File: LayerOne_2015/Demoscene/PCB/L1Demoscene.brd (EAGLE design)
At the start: 50 x 50 mm, 54 parts, among them IC1 MEGA8-AI, IC2 REG1117, J1 AVR_SPI_PRG_6PTH, J2 CON_HEADER_1X02-PTH

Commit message: 
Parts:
- moved C2 1.02 mm to (9.40, 19.3)
- moved R28 0.25 mm to (6.86, 19.3)
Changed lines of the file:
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@@
 </element>
 <element name="C1" library="SparkFun-Capacitors" package="0603-CAP" value="22pF" x="24.638" y="19.304" rot="R270"/>
-<element name="C2" library="SparkFun-Capacitors" package="0603-CAP" value="22pF" x="9.398" y="18.288" rot="R90"/>
+<element name="C2" library="SparkFun-Capacitors" package="0603-CAP" value="22pF" x="9.398" y="19.304" rot="R90"/>
 <element name="R2" library="SparkFun-Resistors" package="0603-RES" value="442" x="28.194" y="2.032"/>
 <element name="R3" library="SparkFun-Resistors" package="0603-RES" value="442" x="34.798" y="4.318"/>
@@
 <element name="C7" library="SparkFun-Capacitors" package="0603-CAP" value="100nf" x="21.336" y="14.986" rot="R225"/>
 <element name="J2" library="dp_devices" package="M1X2" value="CON_HEADER_1X02-PTH" x="2.54" y="33.02" smashed="yes" rot="R270"/>
-<element name="R28" library="SparkFun-Resistors" package="0603-RES" value="1k" x="6.858" y="19.05" rot="R270"/>
+<element name="R28" library="SparkFun-Resistors" package="0603-RES" value="1k" x="6.858" y="19.304" rot="R270"/>
 <element name="LED1" library="dp_devices" package="LED-603" value="" x="7.874" y="23.876" smashed="yes">
 <attribute name="NAME" x="9.525" y="22.606" size="0.8128" layer="25" font="vector" ratio="10" rot="R90"/>
@@
 <wire x1="16.295425" y1="14.413225" x2="14.478" y2="16.23065" width="0.4064" layer="1"/>
 <wire x1="14.478" y1="16.23065" x2="14.478" y2="19.304" width="0.4064" layer="1"/>
-<wire x1="9.398" y1="19.138" x2="9.398" y2="20.574" width="0.4064" layer="1"/>
-<via x="9.398" y="20.574" extent="1-16" drill="0.4572"/>
-<wire x1="9.398" y1="20.574" x2="13.208" y2="20.574" width="0.4064" layer="16"/>
 <wire x1="13.208" y1="20.574" x2="14.478" y2="19.304" width="0.4064" layer="16"/>
+<wire x1="13.208" y1="20.574" x2="12.192" y2="21.59" width="0.4064" layer="16"/>
+<wire x1="12.192" y1="21.59" x2="9.398" y2="21.59" width="0.4064" layer="16"/>
+<via x="9.398" y="21.59" extent="1-16" drill="0.4572"/>
+<wire x1="9.398" y1="21.59" x2="9.398" y2="20.154" width="0.4064" layer="1"/>
 </signal>
 <signal name="VCC">
@@
 <contactref element="R28" pad="1"/>
 <contactref element="LED1" pad="A"/>
-<wire x1="6.858" y1="19.9" x2="6.858" y2="20.828" width="0.4064" layer="1"/>
+<wire x1="6.858" y1="20.154" x2="6.858" y2="20.828" width="0.4064" layer="1"/>
 <wire x1="6.858" y1="20.828" x2="7.874" y2="21.844" width="0.4064" layer="1"/>
 <wire x1="7.874" y1="21.844" x2="7.874" y2="23.126" width="0.4064" layer="1"/>
@@
 <wire x1="10.16" y1="14.986" x2="8.89" y2="14.986" width="0.4064" layer="1"/>
 <wire x1="8.89" y1="14.986" x2="6.858" y2="17.018" width="0.4064" layer="1"/>
-<wire x1="6.858" y1="17.018" x2="6.858" y2="18.2" width="0.4064" layer="1"/>
+<wire x1="6.858" y1="17.018" x2="6.858" y2="18.454" width="0.4064" layer="1"/>
 </signal>
 <signal name="PD0">

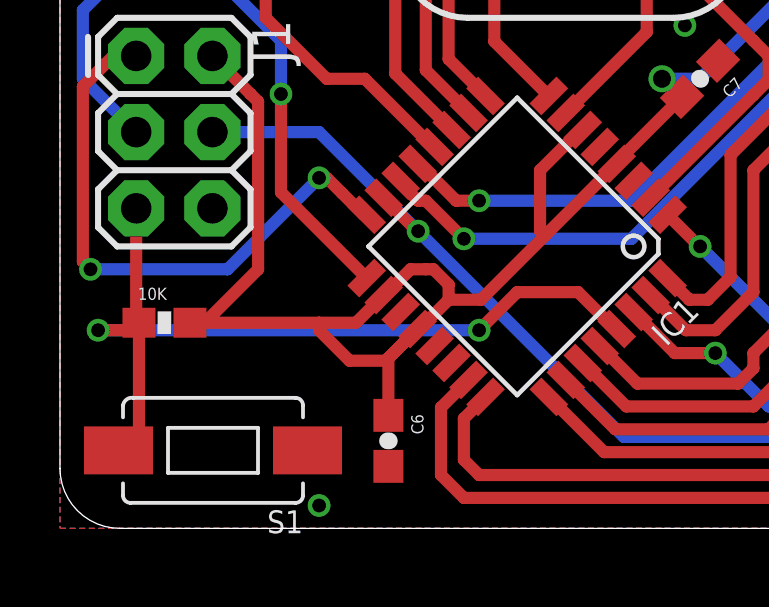
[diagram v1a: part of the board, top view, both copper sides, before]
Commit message: added NC jumper to AVcc pin
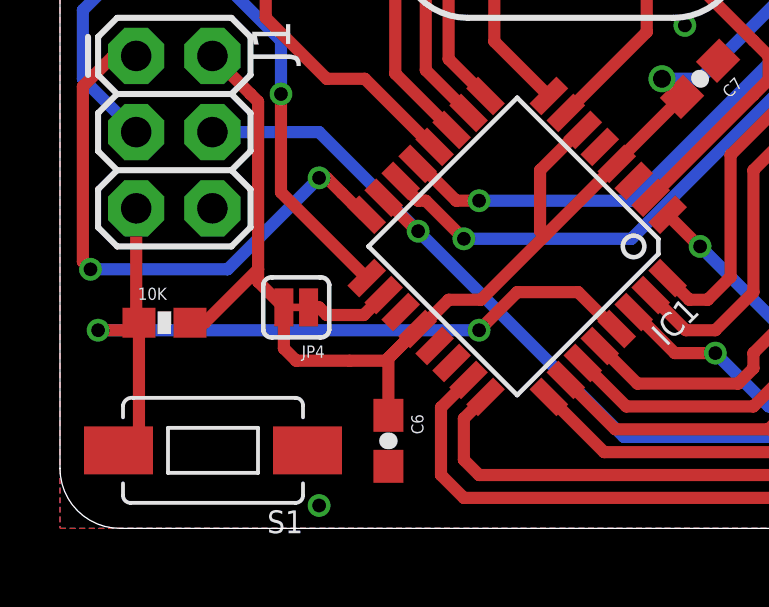
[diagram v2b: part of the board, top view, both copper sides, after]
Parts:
- added JP4: (no value), SparkFun-Passives:SJ_2S
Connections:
- net VCC: now also JP4.1, JP4.2
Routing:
- net VCC: track 84.5 -> 81.7 mm
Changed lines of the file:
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@@
 </element>
 <element name="S2" library="tvbgone-2layer" package="SPARKFUN-ELECTROMECHANICAL_TACTILE-SWITCH-1101NE" value="Switch" x="43.18" y="13.716"/>
+<element name="JP4" library="SparkFun-Passives" package="SJ_2S" value="" x="7.874" y="7.366" rot="R180"/>
 </elements>
 <signals>
@@
 <contactref element="C4" pad="-"/>
 <contactref element="S1" pad="P$1"/>
-<contactref element="C6" pad="2"/>
 <contactref element="C7" pad="1"/>
 <via x="20.828" y="16.764" extent="1-16" drill="0.4572"/>
@@
 <contactref element="LED1" pad="C"/>
 <contactref element="S2" pad="P$1"/>
+<contactref element="C6" pad="2"/>
 </signal>
 <signal name="N$1">
@@
 <contactref element="IC1" pad="4"/>
 <contactref element="IC1" pad="6"/>
-<contactref element="IC1" pad="18"/>
 <contactref element="IC1" pad="20"/>
 <contactref element="10K" pad="2"/>
@@
 <wire x1="6.604" y1="8.636" x2="4.822" y2="6.854" width="0.4064" layer="1"/>
 <wire x1="4.822" y1="6.854" x2="4.332" y2="6.854" width="0.4064" layer="1"/>
-<wire x1="11.684" y1="8.636" x2="10.824884375" y2="7.776884375" width="0.4064" layer="1"/>
-<wire x1="10.824884375" y1="7.776884375" x2="10.790459375" y2="7.776884375" width="0.4064" layer="1"/>
 <wire x1="18.55816875" y1="12.15048125" x2="16.15784375" y2="9.75015625" width="0.4064" layer="1"/>
 <wire x1="16.15784375" y1="9.75015625" x2="14.0276875" y2="7.62" width="0.4064" layer="1"/>
@@
 <wire x1="12.954" y1="7.62" x2="11.979515625" y2="6.645515625" width="0.4064" layer="1"/>
 <wire x1="11.979515625" y1="6.645515625" x2="11.921828125" y2="6.645515625" width="0.4064" layer="1"/>
-<wire x1="10.790459375" y1="7.776884375" x2="9.867575" y2="6.854" width="0.4064" layer="1"/>
-<wire x1="9.867575" y1="6.854" x2="8.636" y2="6.854" width="0.4064" layer="1"/>
-<wire x1="8.636" y1="6.854" x2="4.332" y2="6.854" width="0.4064" layer="1"/>
 <wire x1="11.921828125" y1="6.645515625" x2="11.52815625" y2="6.25184375" width="0.4064" layer="1"/>
 <wire x1="11.52815625" y1="6.25184375" x2="10.8643125" y2="5.588" width="0.4064" layer="1"/>
 <wire x1="10.8643125" y1="5.588" x2="9.652" y2="5.588" width="0.4064" layer="1"/>
-<wire x1="9.652" y1="5.588" x2="8.636" y2="6.604" width="0.4064" layer="1"/>
-<wire x1="8.636" y1="6.604" x2="8.636" y2="6.854" width="0.4064" layer="1"/>
 <wire x1="10.94679375" y1="3.766790625" x2="10.94679375" y2="5.67048125" width="0.4064" layer="1"/>
 <wire x1="10.94679375" y1="5.67048125" x2="11.52815625" y2="6.25184375" width="0.4064" layer="1"/>
@@
 <wire x1="16.002" y1="11.938" x2="16.002" y2="9.906" width="0.4064" layer="1"/>
 <wire x1="16.002" y1="9.906" x2="16.15784375" y2="9.75015625" width="0.4064" layer="1"/>
-<wire x1="11.684" y1="8.636" x2="12.192" y2="8.636" width="0.4064" layer="1"/>
-<wire x1="12.192" y1="8.636" x2="12.446" y2="8.636" width="0.4064" layer="1"/>
-<wire x1="12.446" y1="8.636" x2="12.954" y2="8.128" width="0.4064" layer="1"/>
-<wire x1="12.954" y1="8.128" x2="12.954" y2="7.62" width="0.4064" layer="1"/>
 <wire x1="28.07" y1="28.194" x2="27.94" y2="28.064" width="0.4064" layer="1"/>
 <wire x1="27.94" y1="28.064" x2="27.94" y2="21.59" width="0.4064" layer="1"/>
@@
 <wire x1="15.494" y1="36.068" x2="16.54" y2="35.022" width="0.4064" layer="1"/>
 <wire x1="16.54" y1="35.022" x2="16.54" y2="34.29" width="0.4064" layer="1"/>
+<contactref element="JP4" pad="2"/>
+<wire x1="9.652" y1="5.588" x2="7.874" y2="5.588" width="0.4064" layer="1"/>
+<wire x1="7.874" y1="5.588" x2="7.4621" y2="5.9999" width="0.4064" layer="1"/>
+<wire x1="7.4621" y1="5.9999" x2="7.4621" y2="7.366" width="0.4064" layer="1"/>
+<wire x1="7.4621" y1="7.366" x2="6.604" y2="8.2241" width="0.4064" layer="1"/>
+<wire x1="6.604" y1="8.2241" x2="6.604" y2="8.636" width="0.4064" layer="1"/>
+<contactref element="IC1" pad="18"/>
+<contactref element="JP4" pad="1"/>
+<wire x1="10.790459375" y1="7.776884375" x2="10.125575" y2="7.112" width="0.4064" layer="1"/>
+<wire x1="10.125575" y1="7.112" x2="8.89" y2="7.112" width="0.4064" layer="1"/>
+<wire x1="8.89" y1="7.112" x2="8.636" y2="7.366" width="0.4064" layer="1"/>
+<wire x1="8.636" y1="7.366" x2="8.382" y2="7.366" width="0.4064" layer="1"/>
+<wire x1="8.382" y1="7.366" x2="8.2859" y2="7.366" width="0.4064" layer="1"/>
+<wire x1="8.2859" y1="7.366" x2="7.4621" y2="7.366" width="0.254" layer="1"/>
 </signal>
 <signal name="RESET">

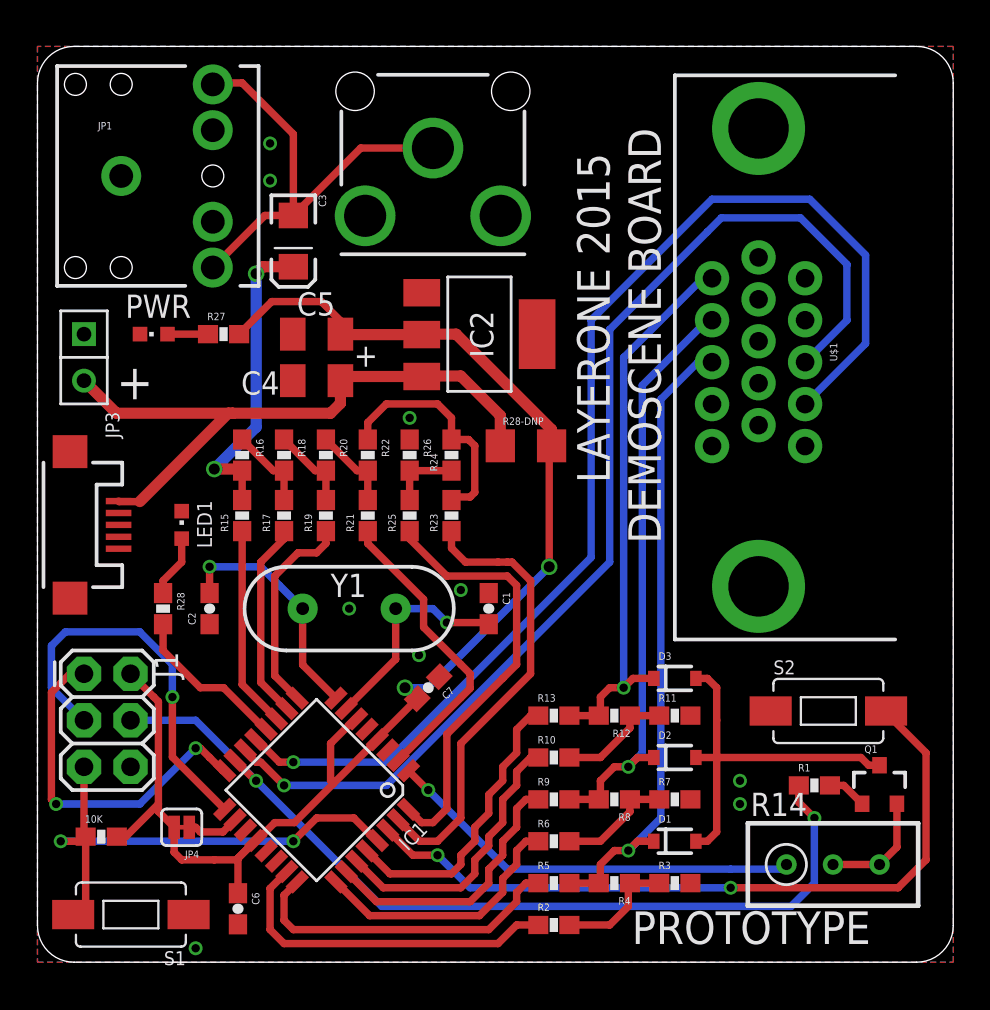
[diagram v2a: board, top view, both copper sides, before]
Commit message: moved aux button
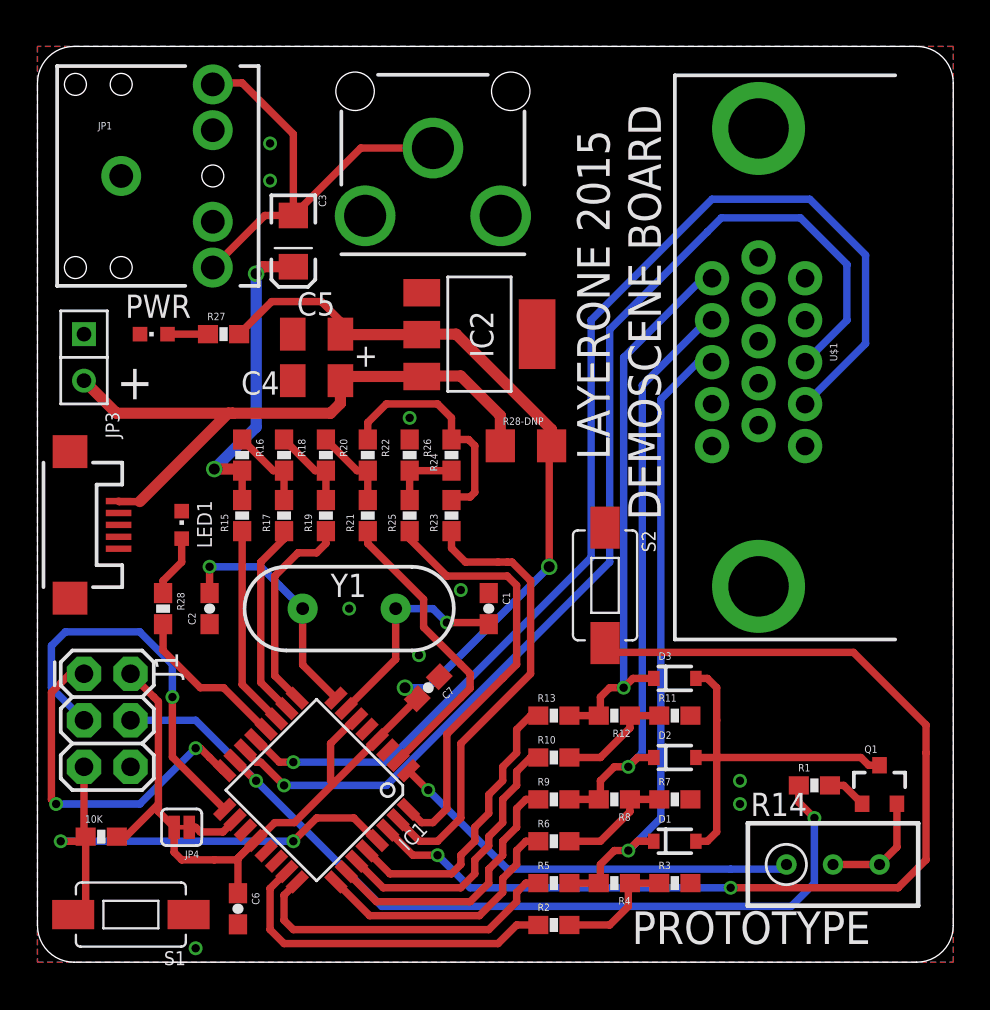
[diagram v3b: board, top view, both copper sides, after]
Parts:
- moved S2 14.0 mm to (31.0, 20.6), turned to 270 degrees
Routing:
- net PD0: track 40.4 -> 58.1 mm
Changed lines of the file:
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@@
 <wire x1="2" y1="0" x2="48" y2="0" width="0" layer="20"/>
 <wire x1="48" y1="0" x2="50" y2="2" width="0" layer="20" curve="90"/>
-<text x="31.242" y="26.162" size="1.778" layer="25" font="vector" rot="R90">LAYERONE 2015</text>
-<text x="34.036" y="22.86" size="1.778" layer="25" font="vector" rot="R90">DEMOSCENE BOARD</text>
+<text x="31.242" y="27.432" size="1.778" layer="25" font="vector" rot="R90">LAYERONE 2015</text>
+<text x="34.036" y="24.13" size="1.778" layer="25" font="vector" rot="R90">DEMOSCENE BOARD</text>
 <text x="32.451484375" y="0.9944875" size="1.778" layer="25" font="vector">PROTOTYPE</text>
 <text x="4.318" y="30.734" size="1.9304" layer="21">+</text>
@@
 <attribute name="VALUE" x="9.779" y="22.606" size="1.27" layer="27" ratio="10" rot="R90"/>
 </element>
-<element name="S2" library="tvbgone-2layer" package="SPARKFUN-ELECTROMECHANICAL_TACTILE-SWITCH-1101NE" value="Switch" x="43.18" y="13.716"/>
+<element name="S2" library="tvbgone-2layer" package="SPARKFUN-ELECTROMECHANICAL_TACTILE-SWITCH-1101NE" value="Switch" x="30.988" y="20.574" rot="R270"/>
 <element name="JP4" library="SparkFun-Passives" package="SJ_2S" value="" x="7.874" y="7.366" rot="R180"/>
 </elements>
@@
 <wire x1="46.99" y1="4.064" x2="48.514" y2="5.588" width="0.4064" layer="1"/>
 <wire x1="48.514" y1="5.588" x2="48.514" y2="11.43" width="0.4064" layer="1"/>
-<wire x1="48.514" y1="11.43" x2="46.33" y2="13.614" width="0.4064" layer="1"/>
-<wire x1="46.33" y1="13.614" x2="46.33" y2="13.716" width="0.4064" layer="1"/>
+<wire x1="44.552" y1="16.916" x2="48.514" y2="12.954" width="0.4064" layer="1"/>
+<wire x1="48.514" y1="12.954" x2="48.514" y2="11.43" width="0.4064" layer="1"/>
+<wire x1="44.552" y1="16.916" x2="31.496" y2="16.916" width="0.4064" layer="1"/>
+<wire x1="31.496" y1="16.916" x2="30.988" y2="17.424" width="0.4064" layer="1"/>
 </signal>
 </signals>

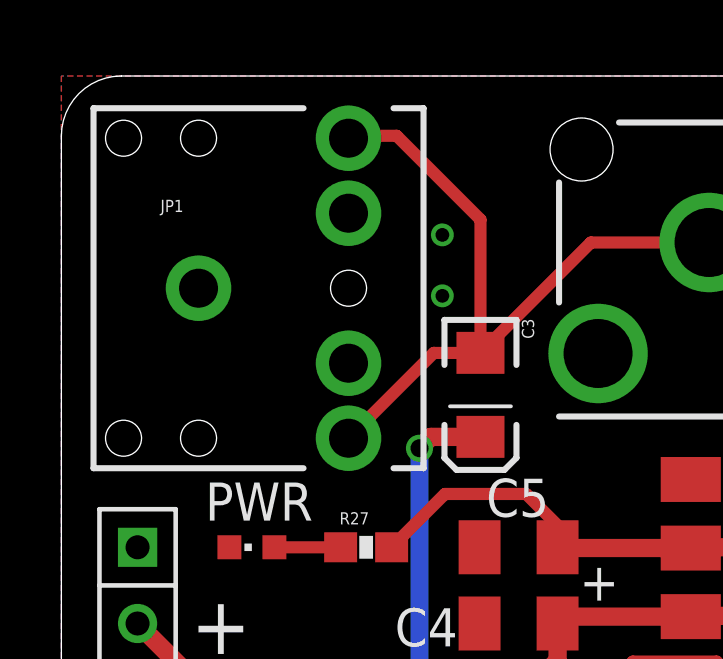
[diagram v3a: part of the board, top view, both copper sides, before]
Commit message: Moved audio jack forward for clearance.
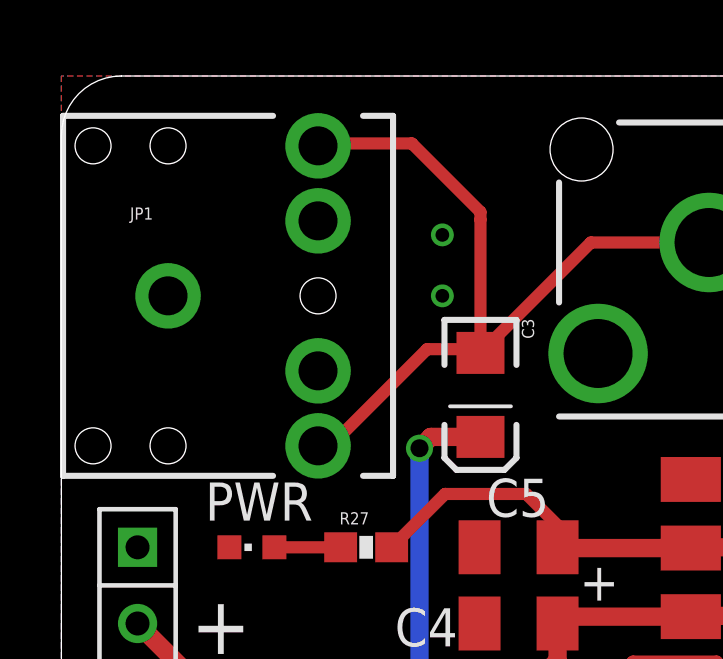
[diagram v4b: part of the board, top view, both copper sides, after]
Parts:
- moved JP1 1.05 mm to (3.56, 42.7)
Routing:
- net AUDIO: track 24.8 -> 27.0 mm
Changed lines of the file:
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@@
 </element>
 <element name="10K" library="SparkFun-Resistors" package="0603-RES" value="" x="3.482" y="6.854"/>
-<element name="JP1" library="SparkFun-Connectors" package="AUDIO-JACK" value="" x="4.572" y="42.926"/>
+<element name="JP1" library="SparkFun-Connectors" package="AUDIO-JACK" value="" x="3.556" y="42.672"/>
 <element name="JP2" library="SparkFun-Connectors" package="RCA" value="RCA" x="21.59" y="44.45" rot="R270"/>
 <element name="JP3" library="STM32-PROX" package="USB-MICROB" value="USB-MICROB" x="1.778" y="23.876" smashed="yes" rot="R270">
@@
 <wire x1="13.97" y1="40.77" x2="17.65" y2="44.45" width="0.4064" layer="1"/>
 <wire x1="17.65" y1="44.45" x2="21.59" y2="44.45" width="0.4064" layer="1"/>
-<wire x1="9.572" y1="37.926" x2="12.416" y2="40.77" width="0.4064" layer="1"/>
-<wire x1="12.416" y1="40.77" x2="13.97" y2="40.77" width="0.4064" layer="1"/>
-<wire x1="9.572" y1="47.926" x2="9.652" y2="48.006" width="0.4064" layer="1"/>
-<wire x1="9.652" y1="48.006" x2="11.176" y2="48.006" width="0.4064" layer="1"/>
-<wire x1="11.176" y1="48.006" x2="13.97" y2="45.212" width="0.4064" layer="1"/>
 <wire x1="13.97" y1="45.212" x2="13.97" y2="40.77" width="0.4064" layer="1"/>
+<wire x1="8.556" y1="37.672" x2="8.97" y2="37.672" width="0.4064" layer="1"/>
+<wire x1="8.97" y1="37.672" x2="12.192" y2="40.894" width="0.4064" layer="1"/>
+<wire x1="12.192" y1="40.894" x2="13.846" y2="40.894" width="0.4064" layer="1"/>
+<wire x1="13.846" y1="40.894" x2="13.97" y2="40.77" width="0.4064" layer="1"/>
+<wire x1="13.97" y1="45.212" x2="13.97" y2="45.466" width="0.4064" layer="1"/>
+<wire x1="13.97" y1="45.466" x2="11.684" y2="47.752" width="0.4064" layer="1"/>
+<wire x1="11.684" y1="47.752" x2="8.636" y2="47.752" width="0.4064" layer="1"/>
+<wire x1="8.636" y1="47.752" x2="8.556" y2="47.672" width="0.4064" layer="1"/>
 </signal>
 <signal name="N$10">
